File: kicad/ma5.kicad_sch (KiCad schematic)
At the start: 96 parts, among them K1 A2F1CSQ12VDC1.6, K2 CONTACTOR, K3 A2F1CSQ12VDC1.6, K4 A2F1CSQ12VDC1.6, K5 A2F1CSQ12VDC1.6, K6 CONTACTOR, K7 A2F1CSQ12VDC1.6, K8 A2F1CSQ12VDC1.6, K9 CONTACTOR, M1 alt, M2 starter, M3 #2 fuel pump, M4 #1 fuel pump, SW1 1-3, SW10 1-3, SW11 push-btn, SW12 1-3, SW13 2-10, SW14 1-3, SW17 1-3, SW20 START, SW21 1-3, SW3 2-10, SW5 1-3, SW9 2-10, U1 #1 coil pack, U3 LRD3-14, U4 AFT EFIS, U5 FWD EFIS, U6 TXPNDR, U7 RADIO, U8 #2 coil pack

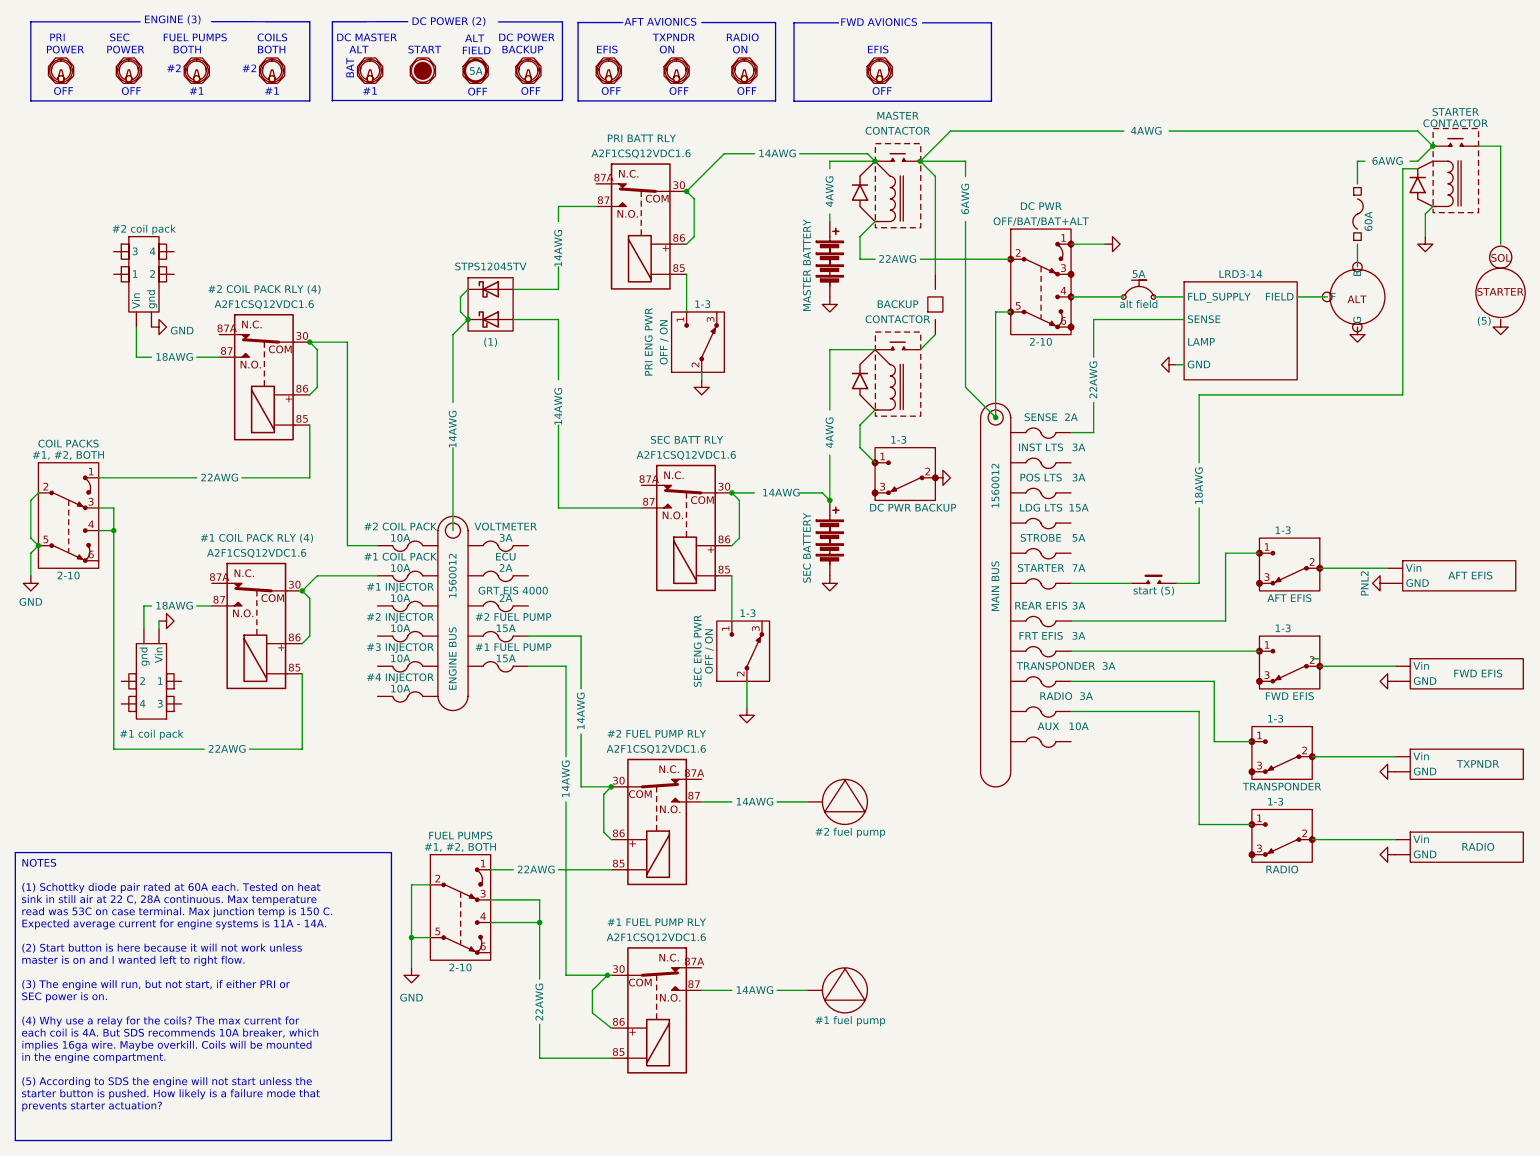
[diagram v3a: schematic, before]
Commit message: Add lights
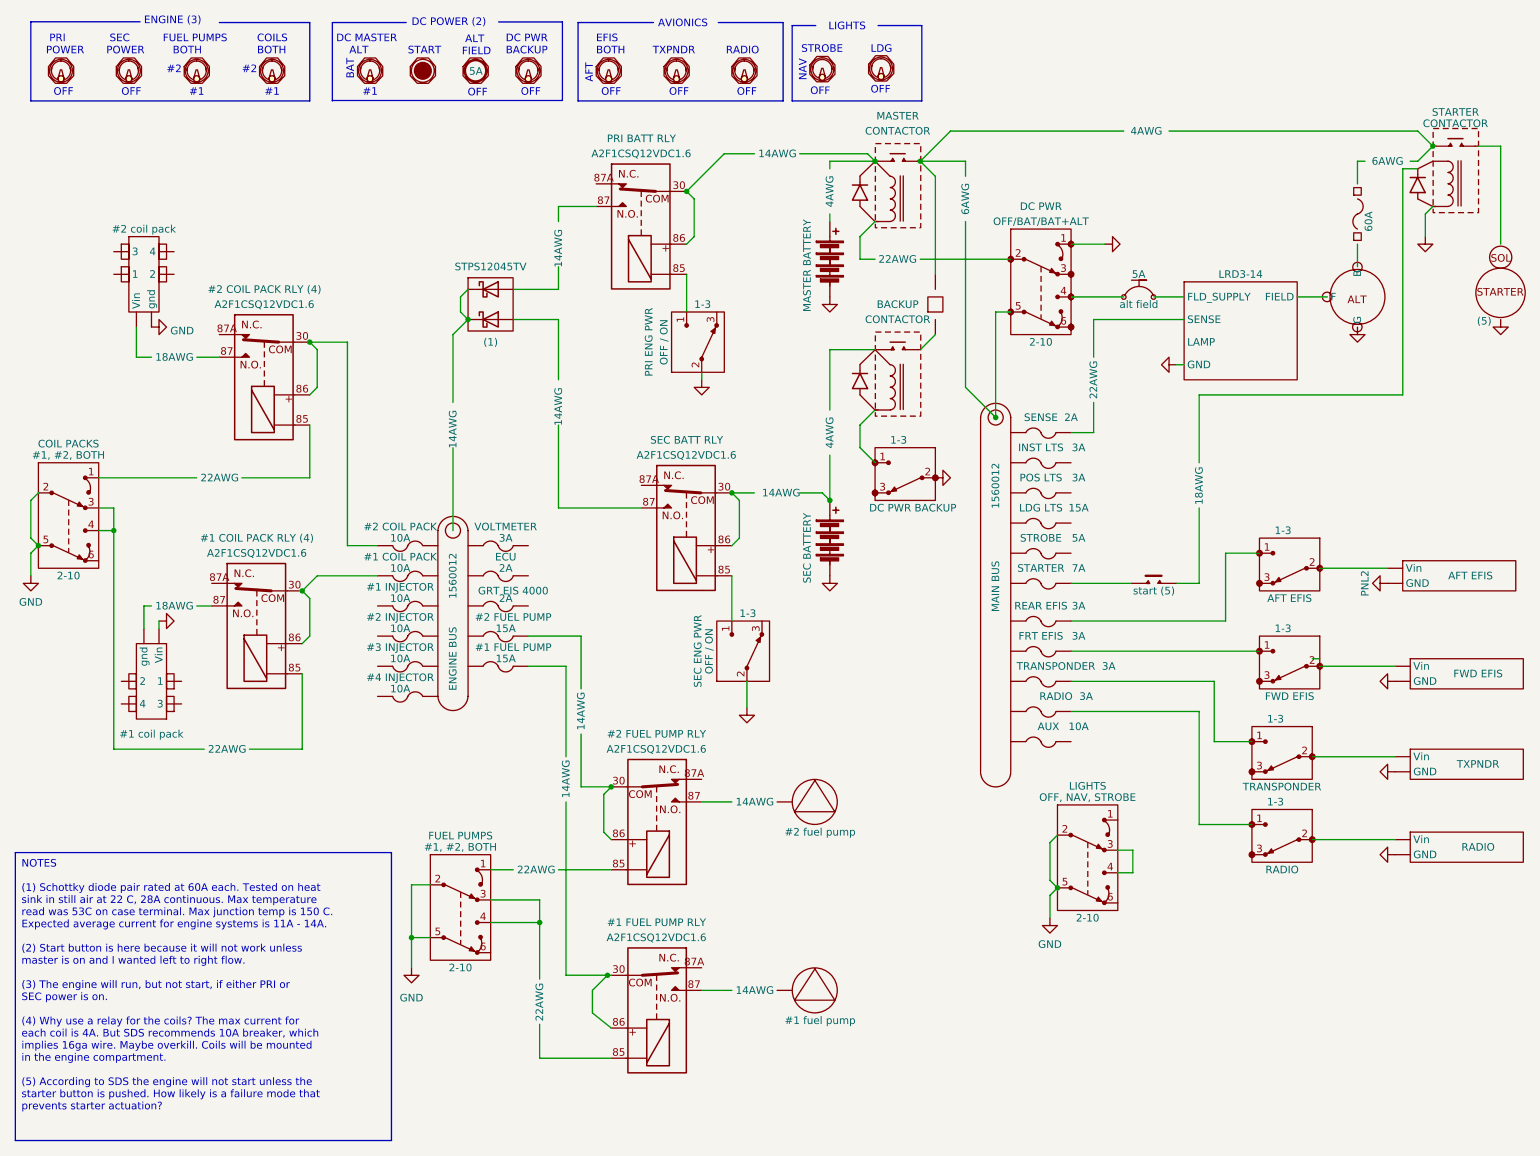
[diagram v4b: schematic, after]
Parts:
- added SW23: ~, symbol ma5_:switch_graphic
- added SW24: 2-10, symbol ma5_:2-10
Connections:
- net GND: now also SW24.2, SW24.5
- net at F4.: now also FB1.5 (5A)
- net at F12.: now also FB1.7 (5A)
- net at F1.: now also F26.; no longer M1. (G)
- net at F26.: now also F25., K9.1; no longer F1.
- net at K9.: now also F35.
- net at F35.: now also SW11.1; no longer K9.
- net at CB1.: now also SW13.4; no longer U3. (SENSE)
- new net: BT1.1 (+), F30., F47.
- new net: F29., F48., K2.1
- new net: F1., M1. (G)
- new net: SW24.3, SW24.4
- new net: M1. (G), U3. (SENSE)
- new net: CB1., U3. (SENSE)
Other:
- note added: "AFT"
- note added: "AVIONICS"
- note added: "DC PWR BACKUP"
- note added: "EFIS BOTH"
- note added: "LDG"
- note added: "LIGHTS"
- note added: "NAV"
- note added: "RADIO"
- note added: "STROBE"
- note added: "TXPNDR"
- note removed: "AFT AVIONICS"
- note removed: "DC POWER BACKUP"
- note removed: "EFIS"
- note removed: "FWD AVIONICS"
- note removed: "RADIO ON"
- note removed: "TXPNDR ON"
